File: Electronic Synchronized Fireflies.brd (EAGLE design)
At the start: 100 x 80 mm, 20 parts, among them IC1 NCP1400A, IC2 G2X[2/3]1---PW14, X1 22-23-2121, X2 22-23-2121

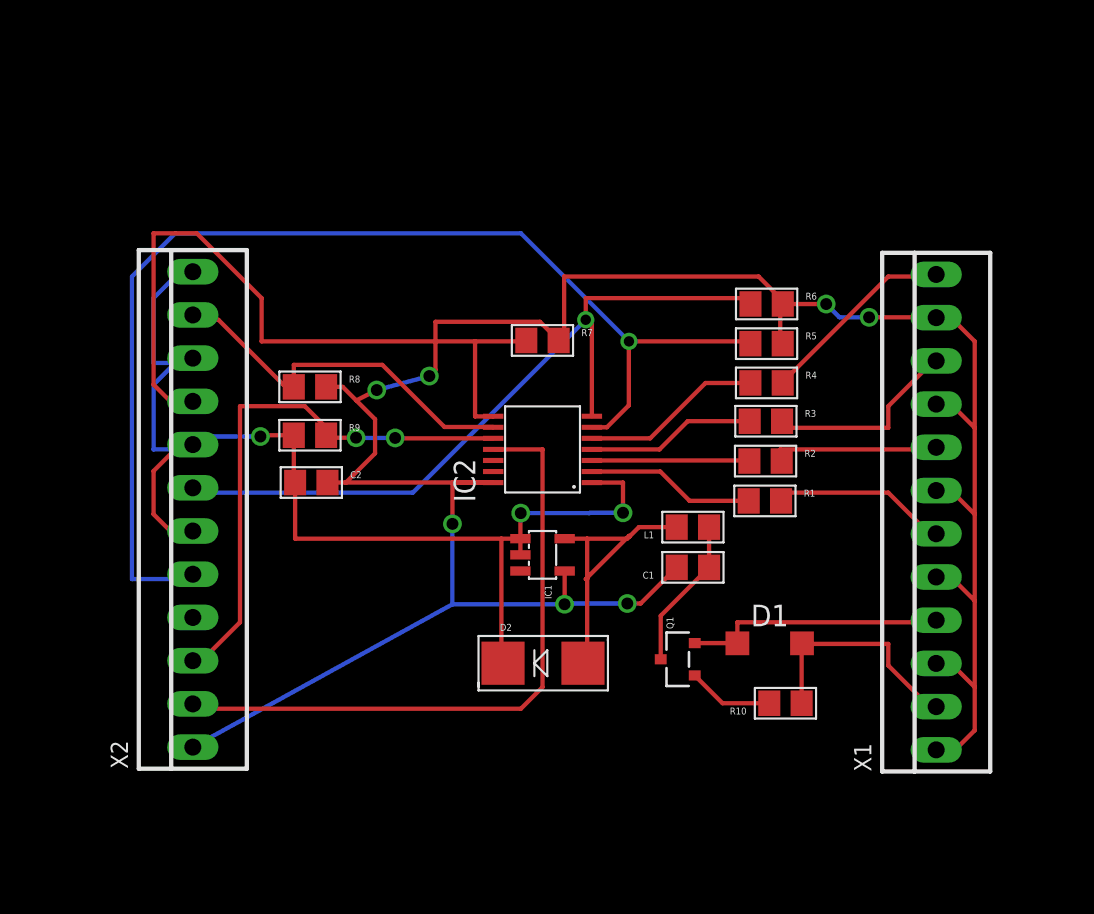
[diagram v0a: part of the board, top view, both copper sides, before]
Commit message: Added power control, PCB improvements
v0.2
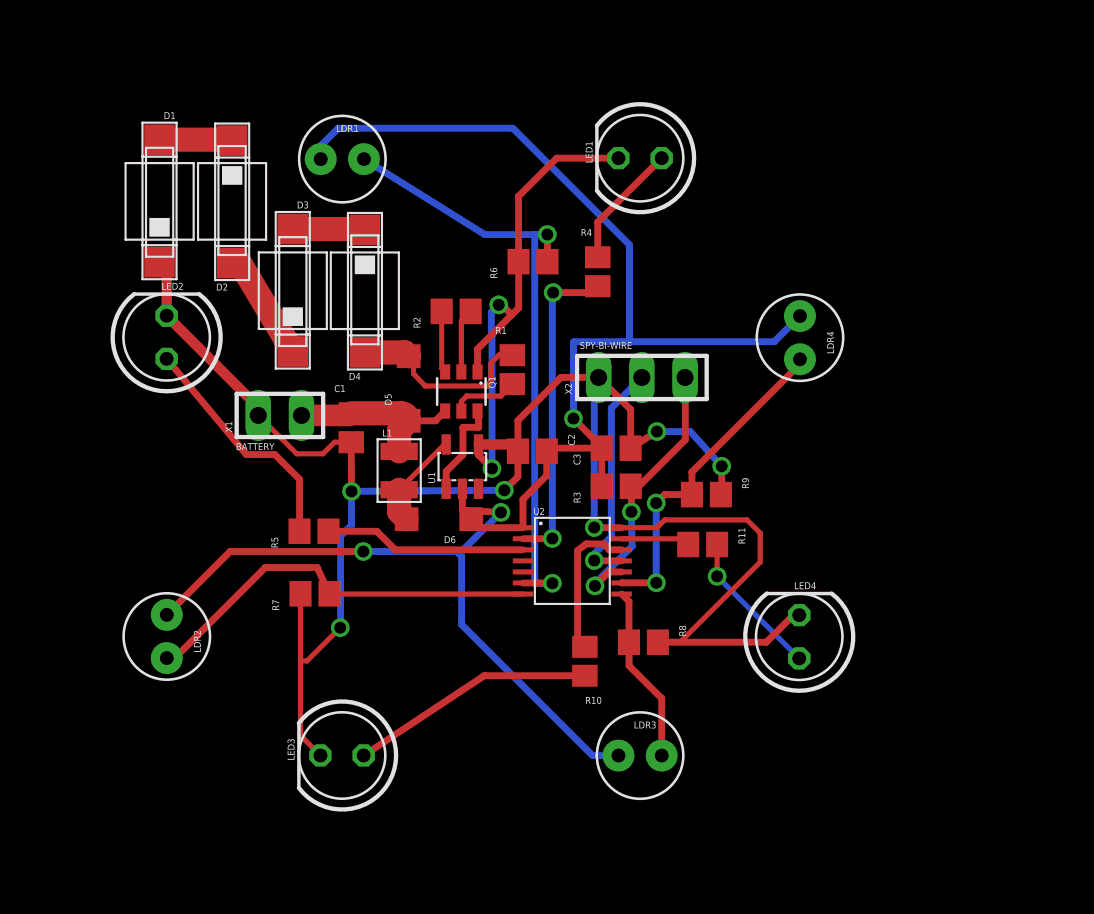
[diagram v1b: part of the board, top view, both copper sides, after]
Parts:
- removed IC1: NCP1400A, microbuilder:SOT23-5
- removed IC2: G2X[2/3]1---PW14, TI_MSP430_v16:PW14
- added C3: 1uF, Firefly:C0805
- added D3, D4: PHOTODIODESMD2, Firefly:PHOTODIODE-SMD2
- added D5, D6: MBR0520LT, Firefly:SOD123
- added LDR1, LDR2, LDR3, LDR4: LDR, Firefly:LDR5MM
- added LED1, LED2, LED3, LED4: (no value), Firefly:LED5MM
- added R11: 56ohm, Firefly:R0805
- added U1: (no value), Firefly:SOT23-5
- added U2: MSP430G2231/TSSOP-14, Firefly:PW14
- C1, C2: device microbuilder:0805 -> Firefly:C0805
- D1: value MBR0520LT -> PHOTODIODESMD2; device diode:SOD123 -> Firefly:PHOTODIODE-SMD2
- D2: value (none) -> PHOTODIODESMD2; device microbuilder:SMADIODE -> Firefly:PHOTODIODE-SMD2
- L1: device microbuilder:0805 -> Firefly:INDUCTOR_1007
- Q1: value (none) -> NPN/PNP; device microbuilder:SOT23-R -> Firefly:SOT363
- R1, R2, R3: value 56ohm -> 20kohm; device microbuilder:0805 -> Firefly:R0805
- R10: value 10kohm -> 56ohm; device microbuilder:0805 -> Firefly:R0805
- R4: device microbuilder:0805 -> Firefly:R0805
- R5: value 22kohm -> 56ohm; device microbuilder:0805 -> Firefly:R0805
- R6, R7, R8: value 22kohm -> 20kohm; device microbuilder:0805 -> Firefly:R0805
- R9: value 10kohm -> 20kohm; device microbuilder:0805 -> Firefly:R0805
- X1: value 22-23-2121 -> 22-23-2021; device con-molex:22-23-2121 -> Firefly:22-23-2021
- X2: value 22-23-2121 -> 22-23-2031; device con-molex:22-23-2121 -> Firefly:22-23-2031
- moved D1 44.4 mm to (24.5, 61.7), turned to 270 degrees
- moved X1 39.0 mm to (31.6, 49.0), turned to 0 degrees
- moved D2 32.6 mm to (28.7, 61.4), turned to 90 degrees
- moved R5 28.8 mm to (33.6, 42.2)
- moved X2 27.5 mm to (52.8, 51.2), turned to 0 degrees
- moved R8 24.7 mm to (52.9, 35.7), turned to 180 degrees
- moved R9 23.6 mm to (56.6, 44.3), turned to 180 degrees
- moved C1 21.7 mm to (35.7, 48.3), turned to 270 degrees
- moved Q1 20.2 mm to (42.2, 50.4), turned to 180 degrees
- moved R2 20.2 mm to (41.9, 55.1)
- moved R7 20.0 mm to (33.6, 38.5)
- moved L1 17.6 mm to (38.6, 45.7), turned to 270 degrees
- moved R1 16.7 mm to (45.2, 51.7), turned to 270 degrees
- moved R6 14.0 mm to (46.4, 58.0)
- moved C2 13.1 mm to (46.4, 46.9), turned to 180 degrees
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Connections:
- new net N$29: LDR3.A, R8.2, U2.8
- new net N$30: LDR4.A, R9.2, U2.9
- new net N$31: LED3.A, R10.1
- new net N$32: LED4.A, R11.1
- net GND: now also C3.2, D1.P$2, LED1.K, LED2.K, LED3.K, LED4.K, Q1.1, R6.1, R7.1, R8.1, R9.1, U1.4, U2.14; no longer IC1.4, IC2.14, R5.2, R6.2, R7.2, R8.2, X1.11, X1.3, X1.5, X1.7, X1.9
- net N$1: now also D1.P$1, D2.P$2; no longer D1.A, R10.1, X1.2
- net N$10: now also Q1.6, U1.1; no longer R2.2, X1.8
- net N$11: now also R4.2, U2.2; no longer R3.2, X1.10
- net N$12: now also R5.2, U2.3; no longer R4.2, X1.12
- net N$13: now also U2.4; no longer IC2.6, R5.1, X2.5
- net N$14: now also R3.2, U2.10, X2.3; no longer IC2.13
- net N$15: now also U2.5; no longer IC2.7, R6.1, X2.7
- net N$16: now also LDR2.A, R7.2, U2.7; no longer IC2.8, R7.1, X2.9
- net N$17: now also LDR1.A, R6.2, U2.6; no longer IC2.9, R8.1, X2.11
- net N$18: now also LED2.A, R5.1; no longer IC2.11, X2.2
- net N$19: now also D3.P$1, D4.P$2; no longer IC2.10, R9.2, X2.3
- net N$2: now also Q1.5, R1.2; no longer D1.C, Q1.2, X1.4
- net N$20: now also U2.11, X2.2; no longer IC2.12
- net N$21: now also R11.2, U2.13; no longer X2.4
- net N$22: now also D4.P$1, D5.A, R1.1; no longer IC1.3
- net N$23: now also R10.2, U2.12; no longer C1.1, L1.1, Q1.3
- net N$24: now also LED1.A, R4.1; no longer Q1.1, R10.2
- net N$3: now also D2.P$1, D3.P$2; no longer D2.A, IC1.5, L1.2
- net N$4: now also C1.1, D5.C, L1.P$1, Q1.4, X1.2; no longer IC2.3, R2.1
- net N$5: now also D6.A, L1.P$2, U1.5; no longer C2.1, D2.C, IC1.1, IC1.2, IC2.1, R9.1, X2.10, X2.12, X2.6, X2.8
- net N$6: now also Q1.3, R2.1; no longer IC2.2, R1.1
- net N$7: now also U1.3; no longer IC2.4, R3.1
- net N$8: now also C2.1, C3.1, D6.C, LDR1.K, LDR2.K, LDR3.K, LDR4.K, R3.1, U1.2, U2.1; no longer IC2.5, R4.1
- net N$9: now also Q1.2, R2.2; no longer R1.2, X1.6
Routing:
- net N$8: track 10.7 -> 105.9 mm, vias 0 -> 3
- net N$13: track 68.9 -> 0.00 mm, vias 1 -> 0
- net N$5: track 70.3 -> 5.78 mm, vias 3 -> 0
- net N$15: track 45.5 -> 0.00 mm, vias 1 -> 0
- net N$19: track 32.6 -> 4.26 mm, vias 2 -> 0
- net N$18: track 38.1 -> 14.1 mm
- net N$30: track 0.00 -> 19.6 mm, vias 0 -> 2
- net N$16: track 43.3 -> 24.1 mm
- net N$14: track 0.00 -> 16.7 mm, vias 0 -> 2
- net N$17: track 22.2 -> 36.9 mm, vias 0 -> 2
- net N$31: track 0.00 -> 14.4 mm
- net N$20: track 0.00 -> 13.5 mm, vias 0 -> 1
- net N$3: track 18.1 -> 6.51 mm
- net N$2: track 15.5 -> 4.01 mm
- net N$22: track 0.00 -> 11.4 mm
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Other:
- board text added: "BATTERY"
- board text added: "SPY-BI-WIRE"

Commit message: Connections for panel, battery, PCB improvements
v0.3 EECS 399 Spring 2012
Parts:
- removed D1, D2, D3, D4: PHOTODIODESMD2, Firefly:PHOTODIODE-SMD2
- added Q2: DMP2035U-7, Firefly:SOT23
- added R12: 20kohm, Firefly:R0805
- added R13, R14, R15, R16, R17: 0ohm, Firefly:R0805
- added TP1, TP2, TP3, TP4, TP5: TPTP08SQ, Firefly:TP08SQ
- added X3: 22-23-2021, Firefly:22-23-2021
- moved R9 5.20 mm to (56.8, 39.1)
- moved R1 4.38 mm to (40.8, 51.9)
- moved C3 3.83 mm to (47.6, 46.1), turned to 90 degrees
- moved R11 3.76 mm to (57.6, 45.0), turned to 270 degrees
- moved R4 3.12 mm to (53.2, 58.3), turned to 180 degrees
- moved Q1 2.73 mm to (44.5, 52.0), turned to 90 degrees
- moved R2 2.27 mm to (44.2, 55.1)
- moved R3 1.93 mm to (49.8, 46.1), turned to 90 degrees
- moved R10 1.73 mm to (49.2, 32.8)
- moved R6 1.26 mm to (47.5, 57.4), turned to 270 degrees
- moved C2 1.26 mm to (45.4, 46.1), turned to 90 degrees
- moved X2 1.25 mm to (52.6, 52.4)
- moved R7 1.17 mm to (33.6, 37.3)
- moved R5 0.93 mm to (32.7, 42.6), turned to 270 degrees
- moved D5 0.66 mm to (38.5, 50.9)
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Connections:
- new net N$25: R11.2, R17.1
- new net N$26: R10.2, R16.1
- net GND: now also TP2.TP, X3.1; no longer D1.P$2
- net N$1: now also LDR1.K, LDR2.K, LDR3.K, LDR4.K, Q2.3; no longer D1.P$1, D2.P$2
- net N$11: now also R14.2; no longer R4.2
- net N$12: now also R15.2; no longer R5.2
- net N$13: now also D5.A, R1.1, TP3.TP, X3.2
- net N$15: now also Q2.2, R12.1, R13.1; no longer U2.5
- net N$19: now also R14.1, R4.2; no longer D3.P$1, D4.P$2
- net N$21: now also R17.2; no longer R11.2
- net N$22: now also R15.1, R5.2; no longer D4.P$1, D5.A, R1.1
- net N$23: now also R16.2; no longer R10.2
- net N$3: now also Q2.1, R12.2, TP5.TP, U2.5; no longer D2.P$1, D3.P$2
- net N$4: now also TP4.TP
- net N$8: now also R13.2, TP1.TP; no longer LDR1.K, LDR2.K, LDR3.K, LDR4.K
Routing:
- net N$8: track 105.9 -> 17.3 mm, vias 3 -> 0
- net N$1: track 4.29 -> 92.6 mm
- net N$13: track 0.00 -> 24.8 mm, vias 0 -> 2
- net N$14: track 16.7 -> 32.1 mm
- net N$11: track 19.0 -> 29.8 mm
- net N$4: track 10.9 -> 21.4 mm, vias 0 -> 2
- net N$22: track 11.4 -> 2.29 mm
- net N$30: track 19.6 -> 28.2 mm, vias 2 -> 1
- net N$32: track 8.69 -> 16.9 mm, vias 1 -> 0
- net N$3: track 6.51 -> 11.6 mm
- net N$12: track 11.9 -> 16.6 mm, vias 0 -> 2
- net N$15: track 0.00 -> 4.69 mm
- net GND: track 145.8 -> 150.3 mm, vias 8 -> 5
- net N$23: track 8.72 -> 13.0 mm, vias 0 -> 2
- net N$17: track 36.9 -> 40.7 mm, vias 2 -> 0
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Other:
- board size 100 x 80 mm -> 45 x 45 mm
- board text added: "ESF399 V4 23MAR2011"
- board text added: "SOLAR CELL"

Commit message: Added test points, MOSFET switch, 0R resistors.
v1.0 First run PCB
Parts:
- removed R17: 0ohm, Firefly:R0805
- Q1: value NPN/PNP -> NPN; device Firefly:SOT363 -> Firefly:SOT23
- R11, R5: value 56ohm -> 20kohm
- R12: value 20kohm -> 0ohm
- R3, R9: value 20kohm -> 56ohm
- moved R4 25.8 mm to (32.7, 42.6), turned to 270 degrees
- moved R6 24.5 mm to (33.6, 37.3), turned to 0 degrees
- moved R14 24.3 mm to (33.6, 39.5), turned to 0 degrees
- moved R5 20.9 mm to (47.5, 57.4)
- moved R13 20.5 mm to (50.0, 57.5), turned to 270 degrees
- moved R7 19.4 mm to (52.9, 35.7), turned to 180 degrees
- moved R11 19.0 mm to (40.5, 36.7), turned to 0 degrees
- moved R10 14.8 mm to (57.6, 45.0), turned to 270 degrees
- moved R15 14.3 mm to (47.0, 34.5), turned to 90 degrees
- moved R3 12.7 mm to (53.2, 58.3), turned to 180 degrees
- moved R16 12.2 mm to (56.8, 41.8), turned to 180 degrees
- moved R2 10.7 mm to (49.8, 46.1), turned to 90 degrees
- moved R9 9.90 mm to (49.2, 32.8), turned to 90 degrees
- moved R8 5.23 mm to (56.8, 39.1)
- moved R12 2.60 mm to (40.6, 39.3)
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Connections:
- removed net N$22 (its old number): R15.1, R5.2
- removed net N$25 (its old number): R11.2, R17.1
- removed net N$6: Q1.3, R2.1
- removed net N$9: Q1.2, R2.2
- new net N$19: R13.1, R3.2
- new net N$26: R15.1, R9.2
- net GND: now also Q1.2, R5.1; no longer Q1.1, R9.1
- net N$10: now also Q1.3; no longer Q1.6
- net N$11: now also R13.2; no longer R14.2
- net N$12: now also R14.2; no longer R15.2
- net N$14: now also R2.2; no longer R3.2
- net N$15: now also R11.1; no longer R13.1
- net N$16: now also R6.2; no longer R7.2
- net N$17: now also R5.2; no longer R6.2
- net N$18: now also R4.1; no longer R5.1
- net N$2: now also Q1.1; no longer Q1.5
- net N$21: now also R16.2; no longer R17.2
- net N$23: now also R15.2; no longer R16.2
- net N$24: now also R3.1; no longer R4.1
- net N$29: now also R7.2; no longer R8.2
- net N$3: now also R11.2; no longer R12.2
- net N$30: now also R8.2; no longer R9.2
- net N$31: now also R9.1; no longer R10.1
- net N$32: now also R10.1; no longer R11.1
- net N$4: no longer Q1.4
- net N$8: now also R12.2, R2.1; no longer R13.2, R3.1
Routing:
- net N$4: track 21.4 -> 10.4 mm, vias 2 -> 0
- net N$9: track 5.82 -> 0.00 mm
- net N$6: track 5.25 -> 0.00 mm
- net N$10: track 8.03 -> 11.0 mm
- net N$25 (its old number): track 2.86 -> 0.00 mm
- net N$19: track 0.00 -> 2.40 mm
- net N$22 (its old number): track 2.29 -> 0.00 mm
- net N$26: track 0.00 -> 2.14 mm
- net GND: track 150.3 -> 151.4 mm
- net N$25: track 2.14 -> 2.86 mm
- net N$2: track 2.72 -> 2.15 mm
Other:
- board text added: "ESF399 V3.3 09APR2012"
- board text removed: "ESF399 V4 23MAR2011"
